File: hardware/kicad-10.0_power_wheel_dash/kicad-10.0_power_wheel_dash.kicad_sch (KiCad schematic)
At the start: 22 parts, among them J1 LCD_Module, J2 MicroSD_Module, J3 24V Battery, U1 ESP32-S3-WROOM-1, U2 MAX98357A Module, U3 SN74AHCT125N, U4 MP1584EN Buck Module, U5 MP1584EN Buck Module, U6 MAX98357A Module

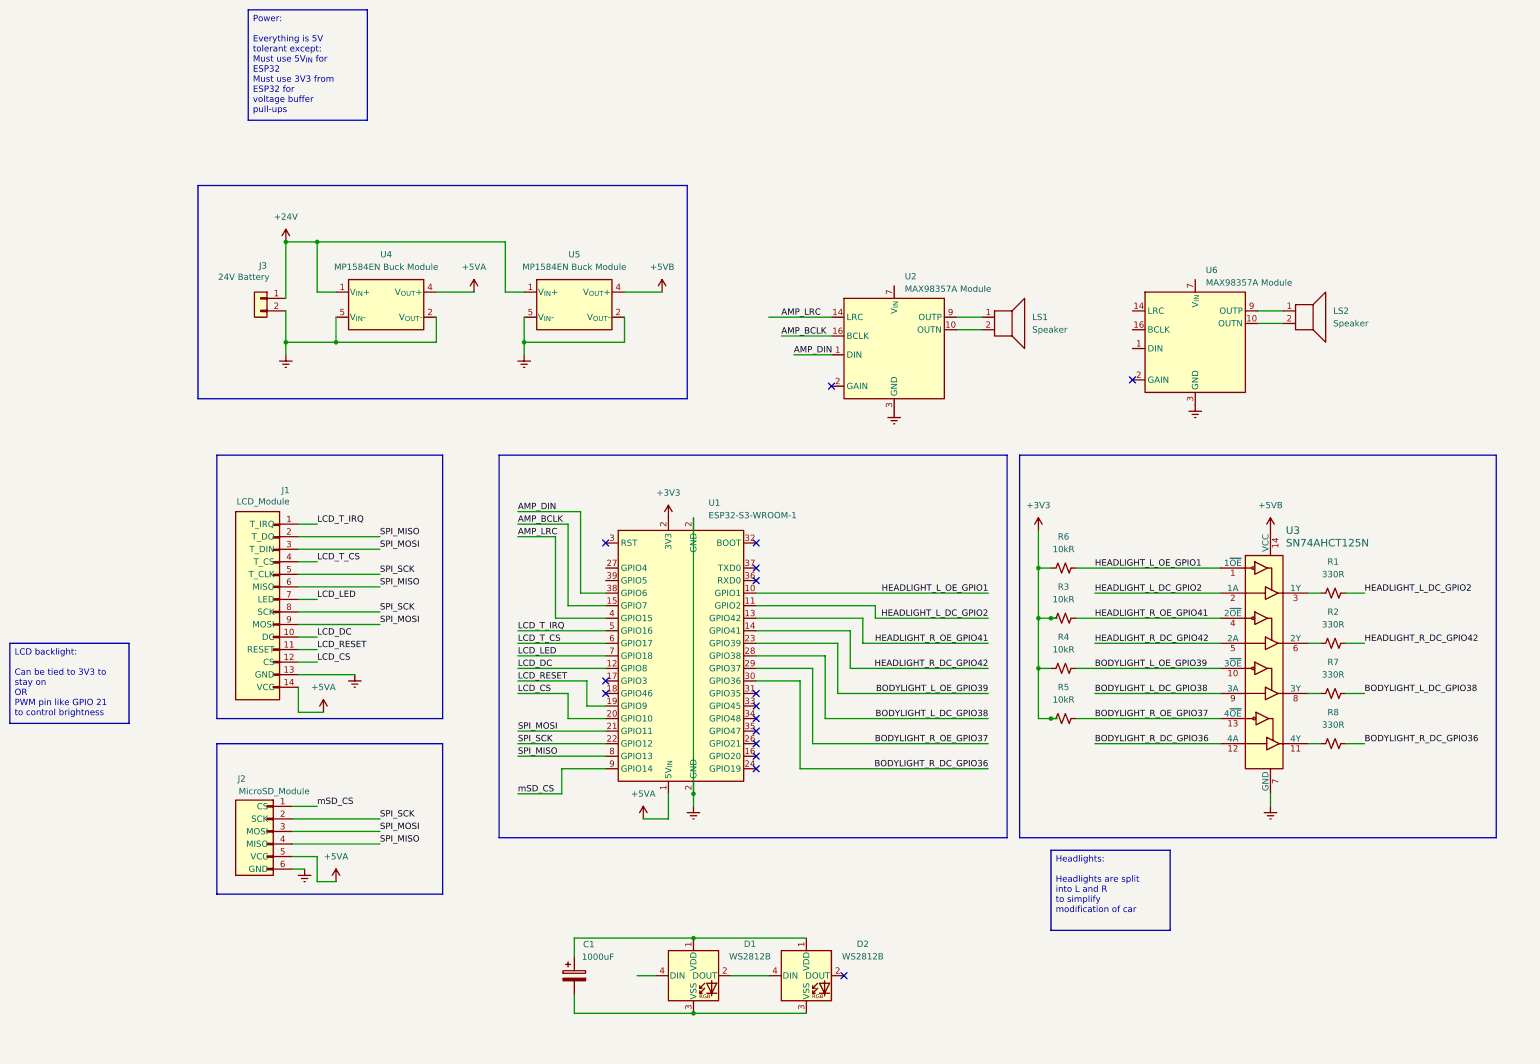
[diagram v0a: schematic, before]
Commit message: fix schematic layout and rename
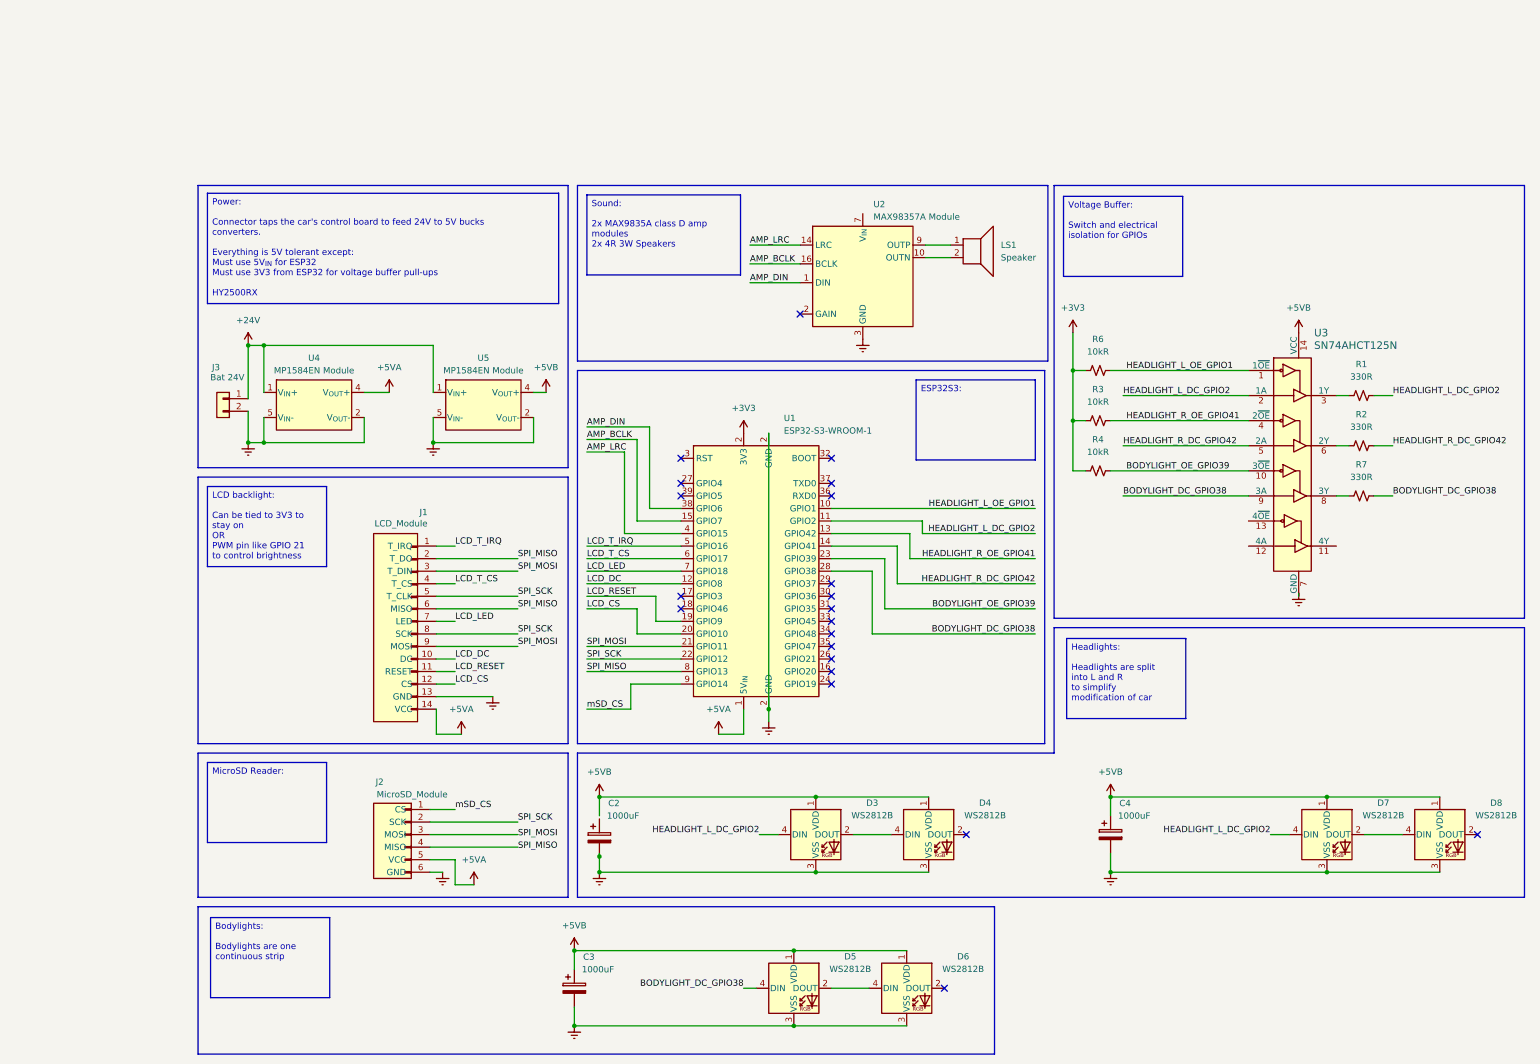
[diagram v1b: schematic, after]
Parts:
- removed C1: 1000uF, symbol Device:C_Polarized
- removed D1, D2: WS2812B, LED_SMD:LED_WS2812B_PLCC4_5.0x5.0mm_P3.2mm, symbol LED:WS2812B
- removed LS2: Speaker, symbol Device:Speaker
- removed R5: 10kR, symbol Device:R_Small_US
- removed R8: 330R, symbol Device:R_Small_US
- removed U6: MAX98357A Module, symbol Audio:MAX98357A
- added C2, C3, C4: 1000uF, symbol Device:C_Polarized
- added D3, D4, D5, D6, D7, D8: WS2812B, LED_SMD:LED_WS2812B_PLCC4_5.0x5.0mm_P3.2mm, symbol LED:WS2812B
- J3: value 24V Battery -> Bat 24V
- U4, U5: value MP1584EN Buck Module -> MP1584EN Module
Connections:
- net +5VB: now also C3.1, C4.1, D3.1 (VDD), D4.1 (VDD), D5.1 (VDD), D6.1 (VDD), D7.1 (VDD), D8.1 (VDD)
- net GNDREF: now also C2.2, C3.2, C4.2, D3.3 (VSS), D4.3 (VSS), D5.3 (VSS), D6.3 (VSS), D7.3 (VSS), D8.3 (VSS)
- net HEADLIGHT_L_DC_GPIO2: now also D3.4 (DIN), D7.4 (DIN)
- net SPI_MISO: no longer J2.4 (MISO)
- net SPI_MOSI: no longer J2.3 (MOSI)
- net BODYLIGHT_L_DC_GPIO38 renamed BODYLIGHT_DC_GPIO38
- net BODYLIGHT_DC_GPIO38: now also D5.4 (DIN)
- net BODYLIGHT_L_OE_GPIO39 renamed BODYLIGHT_OE_GPIO39
- net BODYLIGHT_R_DC_GPIO36: no longer names the net of U1.30 (GPIO36)
- net BODYLIGHT_R_DC_GPIO36: no longer U3.12 (4A)
- net BODYLIGHT_R_OE_GPIO37: no longer names the net of U1.29 (GPIO37)
- net BODYLIGHT_R_OE_GPIO37: no longer U3.13 (4~{OE})
- new net: D7.2 (DOUT), D8.4 (DIN)
- new net: D5.2 (DOUT), D6.4 (DIN)
- new net: D3.2 (DOUT), D4.4 (DIN)
- no-connect marks 16 -> 21
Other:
- title: (none) -> Power Wheel Dashboard
- moved on the sheet: J1, J2, J3, LS1, R1, R2, R3, R4, R6, R7, U1, U2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
